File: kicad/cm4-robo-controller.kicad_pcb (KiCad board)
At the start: 4 copper layers, 150 x 100 mm, 255 parts, among them CN1 SMA-KWE_C7498154, J1 KF7620-7.62-2P, J10 KF2EDGR-2.54-2P, J11 KF7620-7.62-2P, J12 KF2EDGR-2.54-2P, J13 KF2EDGR-2.54-2P, J14 KF7620-7.62-2P, J15 PM254-2-12-Z-8.5, J16 PM254-2-09-Z-8.5, J3 Header-Male-2.54_2x3, J4 2541WV-2X12P, J5 Header-Male-2.54_1x3, J6 Header-Male-2.54_2x3, J7 SMA-KWE_C7498154, J8 KF2EDGR-2.54-4P, J9 KF2EDGR-2.54-3P, Q1 SP40P04NK, Q2 DMP6023LE-13, Q3 NCE6008AS, Q4 BSS138, SW1 SS-12F49-G050, U1 74LVC1G07SE-7, U10 74LVC1G07SE-7, U11 MX26631DL, U12 MAX-M10S-00B, U13 74LVC1G17SE-7, U14 74LVC1G17SE-7, U15 AP64501SP-13, U16 74LVC1G17SE-7, U17 74LVC1G07SE-7, U18 TPS70933DBVR, U19 74LVC1G17SE-7, U2 FSUSB42MUX, U3 USB2514B-I/M2, U4 AP22653W6-7, U5 TPD4EUSB30DQAR, U6 TPD4EUSB30DQAR, U8 TPD4EUSB30DQAR, U9 TPD4EUSB30DQAR, X1 24MHz

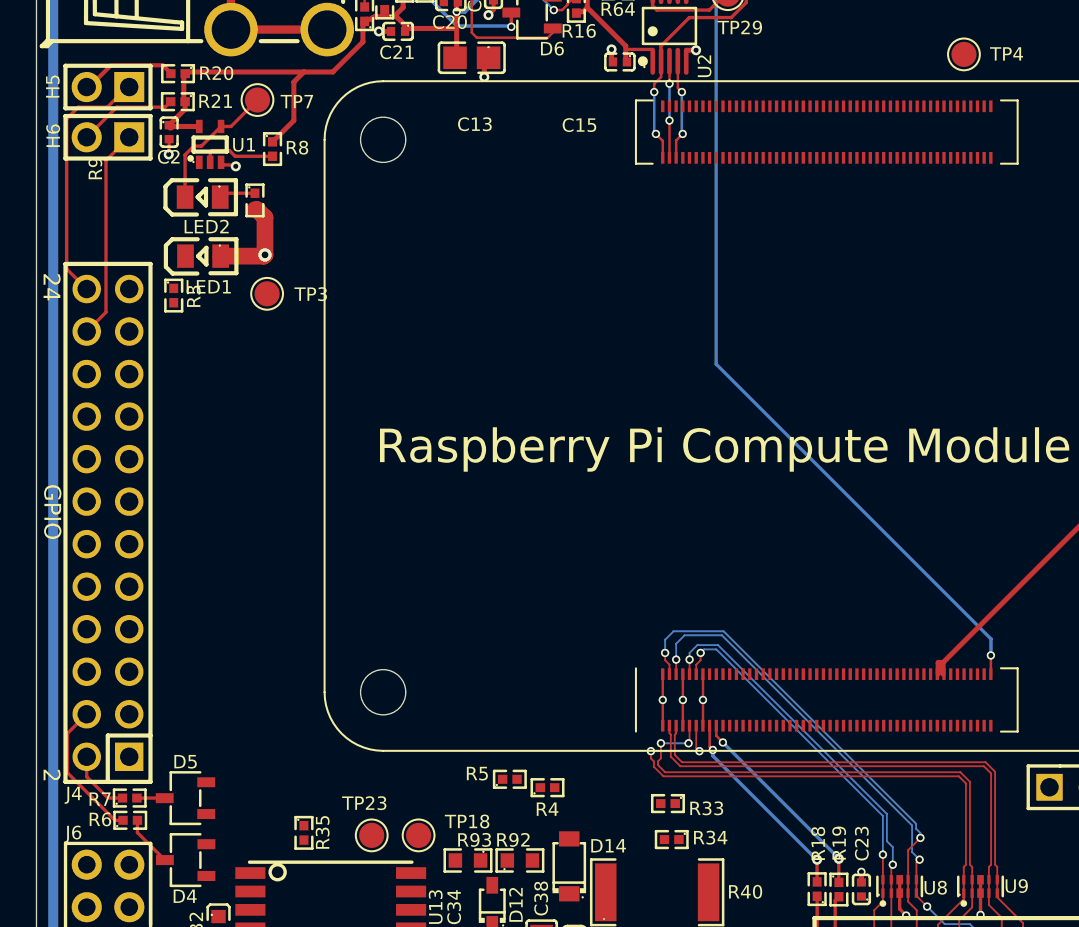
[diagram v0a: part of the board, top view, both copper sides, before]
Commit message: PCB: route J4 GPIO header and R8, move EP0/EP1 bundle east
- Move the EP0/EP1 B.Cu bundle to run east under the CM4 and drop
  straight down at the unused connector pins 61-76 (pairs, vias and
  endpoints unchanged), freeing B.Cu under the GPIO block.
- J4: CM4 inner-row GPIO/SPI as an F.Cu staircase into the J4 inner
  column; outer-row GPIO/SPI via B.Cu channels and a 7-lane ribbon (clear
  of the CM4 mounting-hole keep-out) into the J4 outer column; GPIO17 and
  I2C1 SCL/SDA via B.Cu into J4.20/22/24; J4.5 tied to 3V3.
- R8: nPWR_LED from CM4 pin 95.
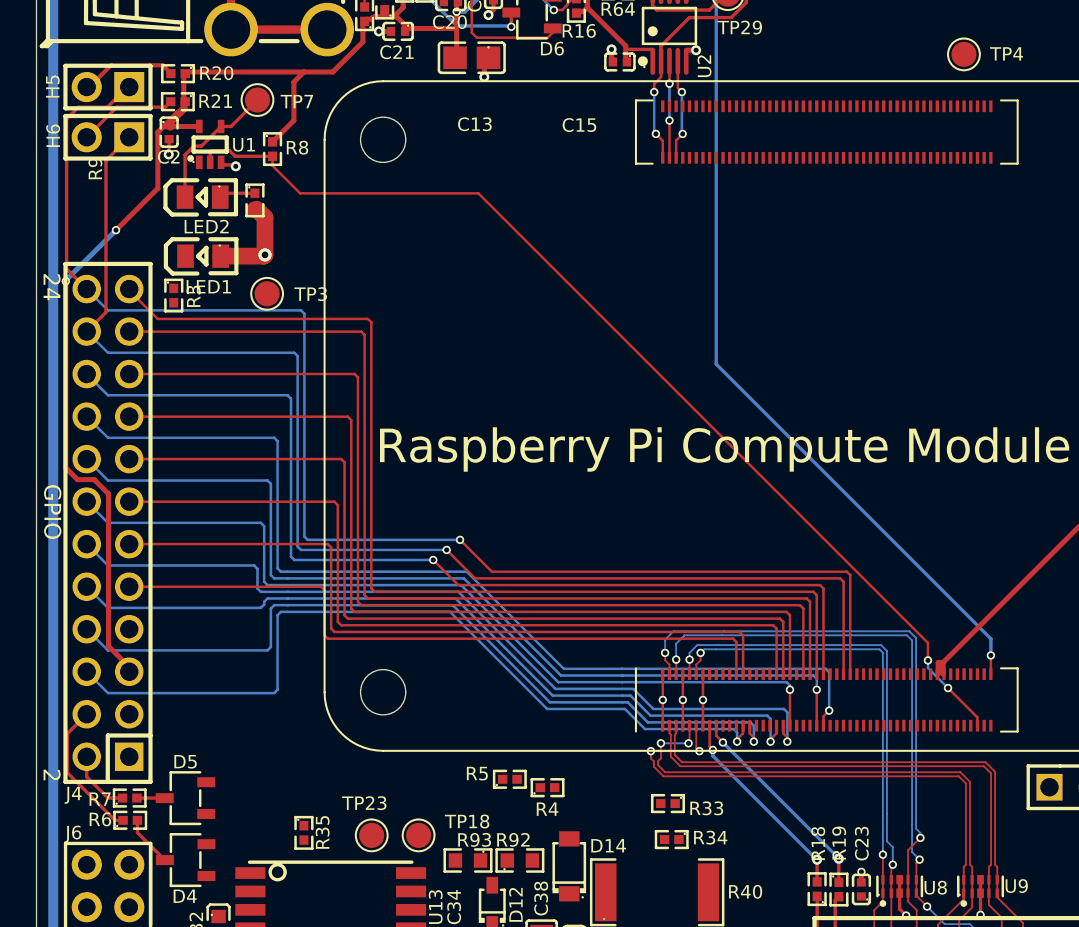
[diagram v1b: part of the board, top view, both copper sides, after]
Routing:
- net /CM4/I2C1_SDA: track 15.2 -> 81.0 mm, vias 0 -> 1
- net /CM4/I2C1_SCL: track 12.7 -> 75.6 mm, vias 0 -> 1
- net /CM4/GPIO27: track 0.00 -> 62.1 mm
- net /CM4/GPIO22: track 0.00 -> 60.8 mm
- net /CM4/GPIO17: track 0.00 -> 59.4 mm, vias 0 -> 1
- net /CM4/GPIO18: track 0.00 -> 57.9 mm, vias 0 -> 1
- net /CM4/SPI0_MOSI: track 0.00 -> 57.8 mm
- net /CM4/nPWR_LED: track 4.51 -> 62.0 mm, vias 0 -> 2
- net /CM4/SPI0_MISO: track 0.00 -> 54.5 mm
- net /CM4/GPIO23: track 0.00 -> 54.4 mm, vias 0 -> 1
- net /CM4/SPI0_SCLK: track 0.00 -> 51.6 mm
- net /CM4/SPI0_CE0: track 0.00 -> 50.3 mm, vias 0 -> 1
- net /CM4/SPI0_CE1: track 0.00 -> 48.9 mm, vias 0 -> 1
- net /CM4/GPIO0: track 0.00 -> 48.6 mm
- net /CM4/GPIO21: track 0.00 -> 48.0 mm, vias 0 -> 1
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
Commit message: PCB: GPS placement and routing, AIP0/AIP1, CM4 GPIO_VREF
- U12 centred between CN1 and J7 with RF_IN facing CN1; GPS parts regrouped by function
- GPS routed: 50 ohm RF_IN (new RF_50_OHM net class, 0.18 mm), antenna bias, backup
  charger, VCC and 3V3 feed, UART to R4/R5, PPS/LED, ext-1PPS input via U13, test points
- F.Cu GND area under U12 stitched to In1
- GPIO4, GPIO5 and 1PPS routed to the CM4; GPIO20/GPIO1 J4 vias nudged apart for 1PPS
- AIP0/AIP1 routed to D5/D4; CM4 pin 78 (GPIO_VREF) tied to 3V3; nPWR_LED via moved north
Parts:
- moved R40 26.2 mm to (72.2, 134.8), turned to 90 degrees
- moved D14 20.1 mm to (75.4, 136.6)
- moved TP18 19.9 mm to (92.3, 140.6)
- moved BT1 19.5 mm to (74.0, 123.4)
- moved TP23 19.4 mm to (88.5, 140.6), turned to 0 degrees
- moved R93 16.9 mm to (72.8, 129.9), turned to 180 degrees
- moved C35 16.6 mm to (85.4, 125.6), turned to 90 degrees
- moved TP20 16.5 mm to (83.6, 121.5)
- moved TP21 16.5 mm to (81.9, 129.6), turned to 0 degrees
- moved R35 14.7 mm to (90.5, 124.6)
- moved C38 14.5 mm to (77.5, 137.3)
- moved C37 14.5 mm to (79.3, 137.3), turned to 90 degrees
- moved C33 14.4 mm to (82.0, 125.6), turned to 90 degrees
- moved R38 13.6 mm to (99.4, 137.0), turned to 90 degrees
- moved C32 13.6 mm to (79.8, 121.6), turned to 0 degrees
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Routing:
- net /CM4/AIP1: track 3.05 -> 63.0 mm, vias 0 -> 4
- net /CM4/AIP0: track 1.66 -> 60.6 mm, vias 0 -> 4
- net /GPS/VCC: track 0.00 -> 40.2 mm, vias 0 -> 2
- net /3V3_CM4: track 284.1 -> 318.4 mm, vias 18 -> 20
- net Net-(Module1A-GPIO4): track 0.00 -> 28.5 mm, vias 0 -> 2
- net GND: track 85.3 -> 112.2 mm, vias 101 -> 133
- net /GPS/EXT_1PPS: track 0.00 -> 24.2 mm, vias 0 -> 2
- net /GPS/V_BCKP: track 0.00 -> 23.7 mm
- net Net-(Module1A-GPIO5): track 0.00 -> 16.7 mm, vias 0 -> 2
- net /CM4/1PPS_MCU: track 0.00 -> 14.8 mm, vias 0 -> 2
- net /GPS/TIMEPULSE: track 0.00 -> 14.5 mm, vias 0 -> 2
- net /GPS/RF_IN: track 0.00 -> 11.0 mm
- net Net-(D14-K): track 0.00 -> 10.4 mm
- net /CM4/ROBO_TX_MCU: track 6.29 -> 0.00 mm, vias 1 -> 0
- net Net-(D13-A): track 0.00 -> 5.62 mm
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
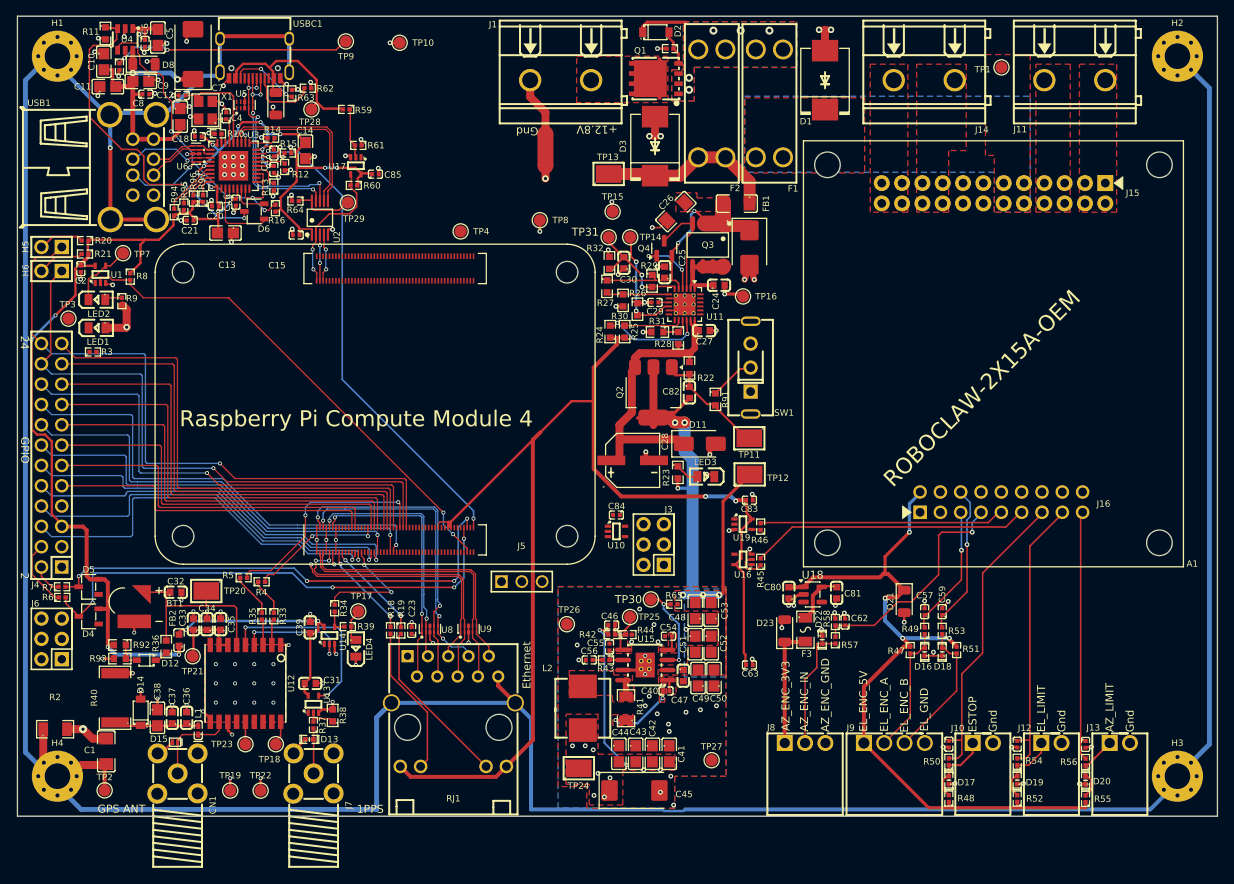
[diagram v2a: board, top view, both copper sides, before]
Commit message: PCB: route remaining CM4 connections, move status LEDs, defer J4
- Remove all J4<->CM4 GPIO tracks; J4 will be routed in a later step
- Route EEPROM_nWP, nPWR_CYCLE, ROBO_RX/TX, BOOT_CONSOLE RXD/TXD,
  PI_nLED_Activity and nPWR_LED; keep F.Cu north of the inner row
  free for the J4 inner-row pins
- Connect CM4 5V pins 77-87 (bar + 3 vias) and all CM4 GND pins
- Join the two 3V3_CM4 islands with a 0.5 mm bridge from C85
- Move LED1/R3/TP3 and LED2/R9/U1/R8/C2/TP7 above RJ1; jog the 3V3
  trunk round J5 (fixes its 0.11 mm clearance to J5 pin 3)
- D4/D5 GND connection
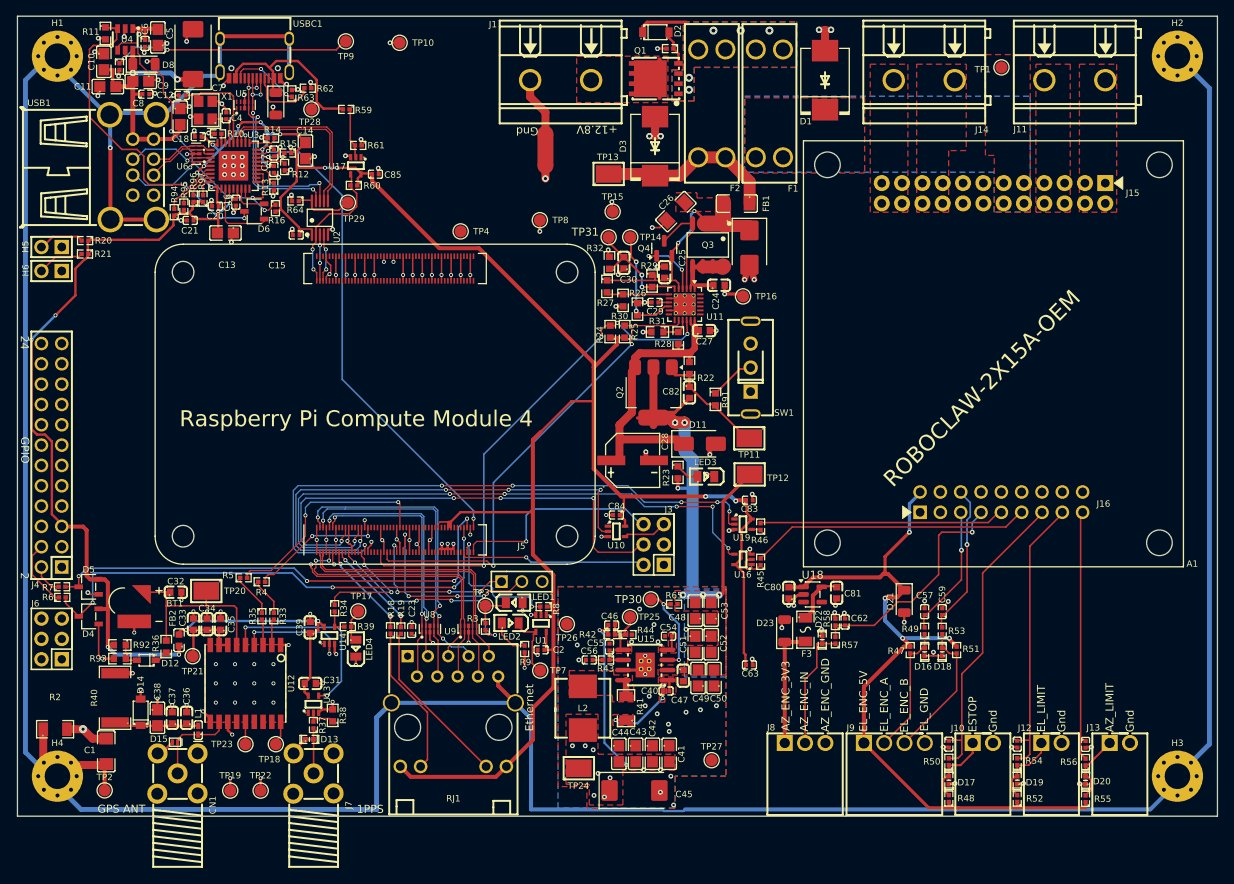
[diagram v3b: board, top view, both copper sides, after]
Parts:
- moved C2 74.7 mm to (125.5, 128.8), turned to 180 degrees
- moved TP7 73.8 mm to (125.3, 131.4)
- moved U1 70.3 mm to (125.5, 125.5), turned to 180 degrees
- moved R9 66.5 mm to (123.4, 128.7)
- moved R8 66.1 mm to (125.8, 123.4), turned to 180 degrees
- moved LED2 65.6 mm to (121.6, 125.5), turned to 180 degrees
- moved TP3 63.3 mm to (118.5, 123.3)
- moved LED1 62.4 mm to (122.1, 122.9)
- moved R3 59.9 mm to (118.5, 125.9), turned to -90 degrees
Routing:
- net /CM4/I2C1_SDA: track 81.0 -> 0.00 mm, vias 1 -> 0
- net /CM4/ROBO_TX_MCU: track 0.00 -> 76.4 mm, vias 0 -> 6
- net /CM4/I2C1_SCL: track 75.6 -> 0.00 mm, vias 1 -> 0
- net /CM4/ROBO_RX_MCU: track 0.00 -> 75.0 mm, vias 0 -> 6
- net /CM4/GPIO27: track 62.1 -> 0.00 mm
- net /CM4/EEPROM_nWP: track 0.00 -> 61.7 mm, vias 0 -> 4
- net /CM4/nPWR_CYCLE: track 0.00 -> 61.4 mm, vias 0 -> 4
- net /CM4/GPIO22: track 60.8 -> 0.00 mm
- net GND: track 112.2 -> 172.7 mm, vias 133 -> 161
- net /CM4/GPIO17: track 59.4 -> 0.00 mm, vias 1 -> 0
- net /CM4/GPIO18: track 57.9 -> 0.00 mm, vias 1 -> 0
- net /CM4/SPI0_MOSI: track 57.8 -> 0.00 mm
- net /CM4/SPI0_MISO: track 54.5 -> 0.00 mm
- net /CM4/GPIO23: track 54.4 -> 0.00 mm, vias 1 -> 0
- net /CM4/~{FLT}: track 7.16 -> 58.9 mm, vias 0 -> 2
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
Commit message: J4 outer row to GND, route SPI0 CE0/CE1, PCB review fixes
Schematic: J4 pins 6, 8, 10, 16, 18 (GPIO21, GPIO20, GPIO1, GPIO23,
GPIO18) are now GND; CM4 pins 25, 27, 35, 47, 49 get no-connect flags.
The five labels, wires and CM4_Connectors sheet pins are removed.

PCB: J4 pad nets updated to match, SPI0_CE0 and SPI0_CE1 routed to the
CM4, the 11 inner J4 nets restored.

Review fixes:
- PGND: solid zone connections on In1 for J1 pin 2 and the RoboClaw
  BAT- pins (were thermal spokes carrying the motor return).
- FUSE_IN: zone outlines widened below the fuse pads so the Q1 source
  arm is ~4 mm instead of 1.2 mm; two more 1.0 mm vias.
- HD2 pair rerouted as a coupled pair on B.Cu through the USB-A pin
  corridor; HD2_P via moved.
- Second 5V via at the U4 input.
- Pair length matching: meanders on EP0-, EP1-, EP2+, EP3-, USB_HUB_N,
  HSD2-, HD1_N; RJ45 legs end at the pin centres. All pairs within
  0.03 mm.
- RF_IN from CN1 re-routed at the 0.18 mm class width (was 1.0/0.3 mm).

Project: DRC exclusions for the silk-to-edge warnings.
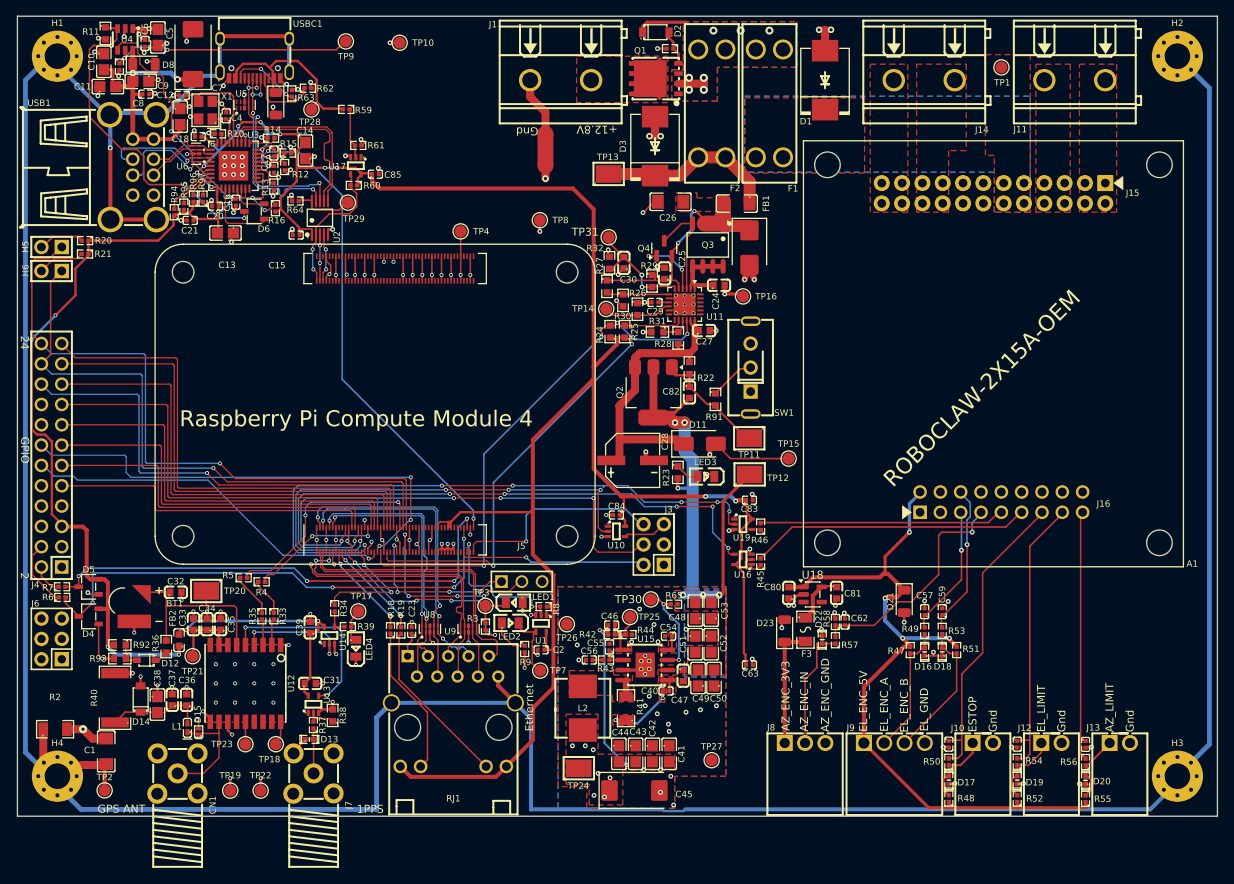
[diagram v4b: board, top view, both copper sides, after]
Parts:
- moved TP15 37.9 mm to (156.4, 104.9)
- moved TP14 9.46 mm to (133.6, 86.2)
- moved D15 3.24 mm to (82.7, 139.0), turned to 90 degrees
- moved C36 2.25 mm to (81.2, 135.1)
- moved C37 2.25 mm to (79.3, 135.1)
- moved C38 1.65 mm to (77.5, 135.7)
- moved D14 1.65 mm to (75.4, 134.9)
- moved C26 1.39 mm to (141.6, 72.8), turned to 0 degrees
- moved L1 1.38 mm to (81.2, 138.6)
- moved C25 0.15 mm to (140.9, 81.8)
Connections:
- J4 pad 10: /CM4/GPIO1 -> GND
- J4 pad 16: /CM4/GPIO23 -> GND
- J4 pad 18: /CM4/GPIO18 -> GND
- J4 pad 6: /CM4/GPIO21 -> GND
- J4 pad 8: /CM4/GPIO20 -> GND
- Module1 pad 25: /CM4/GPIO21 -> unconnected-(Module1A-GPIO21-Pad25)
- Module1 pad 27: /CM4/GPIO20 -> unconnected-(Module1A-GPIO20-Pad27)
- Module1 pad 35: /CM4/GPIO1 -> unconnected-(Module1A-ID_SC-Pad35)
- Module1 pad 47: /CM4/GPIO23 -> unconnected-(Module1A-GPIO23-Pad47)
- Module1 pad 49: /CM4/GPIO18 -> unconnected-(Module1A-GPIO18-Pad49)
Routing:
- net /CM4/I2C1_SDA: track 0.00 -> 81.0 mm, vias 0 -> 1
- net /CM4/I2C1_SCL: track 0.00 -> 75.6 mm, vias 0 -> 1
- net /CM4/GPIO27: track 0.00 -> 62.1 mm
- net /CM4/GPIO22: track 0.00 -> 60.8 mm
- net /CM4/SPI0_CE0: track 0.00 -> 59.6 mm, vias 0 -> 3
- net /CM4/GPIO17: track 0.00 -> 59.4 mm, vias 0 -> 1
- net /CM4/SPI0_MOSI: track 0.00 -> 57.8 mm
- net /CM4/SPI0_MISO: track 0.00 -> 54.5 mm
- net /CM4/SPI0_SCLK: track 0.00 -> 51.6 mm
- net /CM4/GPIO0: track 0.00 -> 48.6 mm
- net /CM4/SPI0_CE1: track 0.00 -> 46.4 mm, vias 0 -> 1
- net /CM4/GPIO19: track 0.00 -> 44.1 mm
- net /CM4/GPIO26: track 0.00 -> 41.1 mm
- net /3V3_CM4: track 353.3 -> 366.1 mm
- net GND: track 172.7 -> 185.1 mm
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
